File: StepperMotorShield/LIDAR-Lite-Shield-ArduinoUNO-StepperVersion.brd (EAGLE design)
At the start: 48 x 59 mm, 10 parts

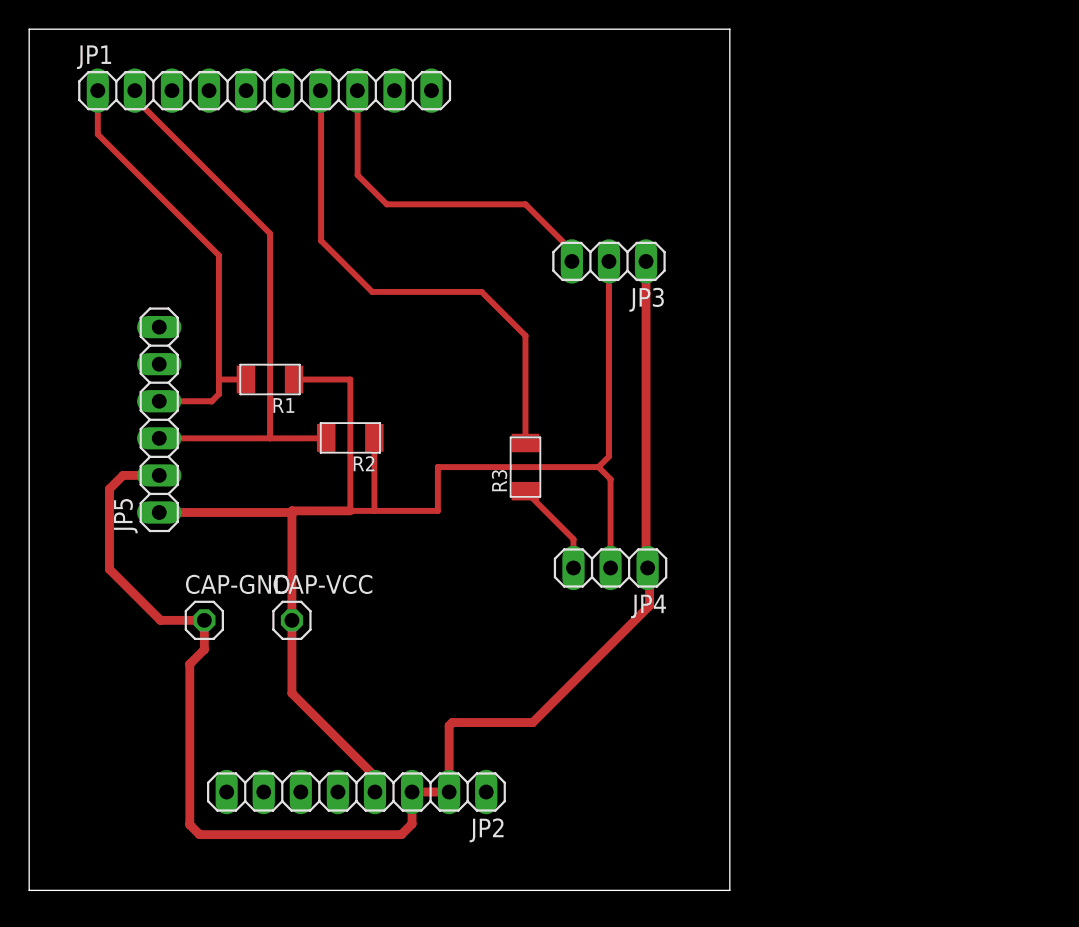
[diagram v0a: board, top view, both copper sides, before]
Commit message: replace Stepper Motor Shiled PCB Design Files to Correct One
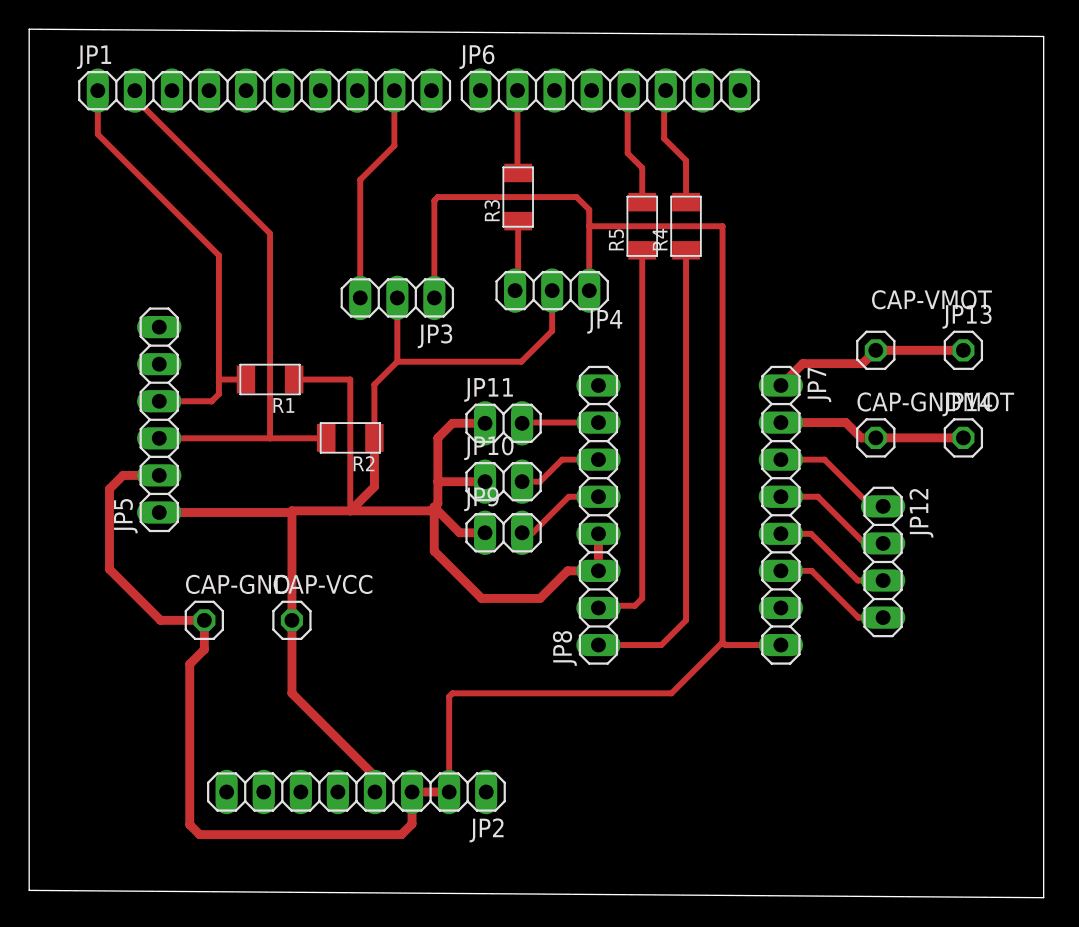
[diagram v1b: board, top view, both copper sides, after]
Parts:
- added CAP-GNDMOT, CAP-VMOT, JP13, JP14: (no value), pinhead:1X01
- added JP10, JP11, JP9: (no value), pinhead:1X02
- added JP12: (no value), pinhead:1X04
- added JP6, JP7, JP8: (no value), pinhead:1X08
- added R4, R5: 0ohm, fab:R1206FAB
- CAP-VCC: value (none) -> 1000uF
- moved JP4 19.4 mm to (35.8, 41.1)
- moved R3 18.5 mm to (33.5, 47.5)
- moved JP3 14.7 mm to (25.2, 40.6)
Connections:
- removed net X-AX: JP1.8, JP3.3
- removed net Y-AX: JP1.7, JP4.3, R3.1, R3.2
- new net 1A: JP12.3, JP7.5
- new net 1B: JP12.2, JP7.4
- new net 2A: JP12.4, JP7.6
- new net 2B: JP12.1, JP7.3
- new net DIR: JP6.6, JP8.1, R4.1, R4.2
- new net ENABLE: JP8.8
- new net FLT: JP7.7
- new net GNDMOT: CAP-GNDMOT.1, JP14.1, JP7.2
- new net M0: JP11.2, JP8.7
- new net M1: JP10.2, JP8.6
- new net M2: JP8.5, JP9.2
- new net STEP: JP6.5, JP8.2, R5.1, R5.2
- new net VMOT: CAP-VMOT.1, JP13.1, JP7.1
- new net YAX1: JP4.3, JP6.2, R3.1, R3.2
- new net YAX2: JP1.9, JP3.3
- net GND: now also JP7.8
- net VCC: now also JP10.1, JP11.1, JP8.3, JP8.4, JP9.1
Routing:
- net GND: track 97.6 -> 144.0 mm
- net Y-AX: track 41.0 -> 0.00 mm
- net DIR: track 0.00 -> 40.4 mm
- net STEP: track 0.00 -> 35.2 mm
- net VCC: track 94.2 -> 118.4 mm
- net X-AX: track 23.4 -> 0.00 mm
- net YAX2: track 0.00 -> 15.2 mm
- net VMOT: track 0.00 -> 13.5 mm
- net GNDMOT: track 0.00 -> 12.9 mm
- net YAX1: track 0.00 -> 10.5 mm
- net 2B: track 0.00 -> 8.33 mm
- net 1B: track 0.00 -> 8.33 mm
- net 2A: track 0.00 -> 8.33 mm
- net 1A: track 0.00 -> 8.33 mm
- net M2: track 0.00 -> 6.25 mm
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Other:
- board size 48 x 59 mm -> 69.5 x 59.5 mm
